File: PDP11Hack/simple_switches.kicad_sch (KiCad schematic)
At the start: 26 parts, among them SW1 SW_SPDT_XKB_DMx-xxxx-1, SW2 SW_SPDT_XKB_DMx-xxxx-1, SW3 SW_Push, SW4 SW_Push, SW5 SW_SPDT_XKB_DMx-xxxx-1, U11_17 74HCT00, U16 74HC14, U17 74HCT00, U18 74HCT00, U20_19 74LS74, U9 74HCT04

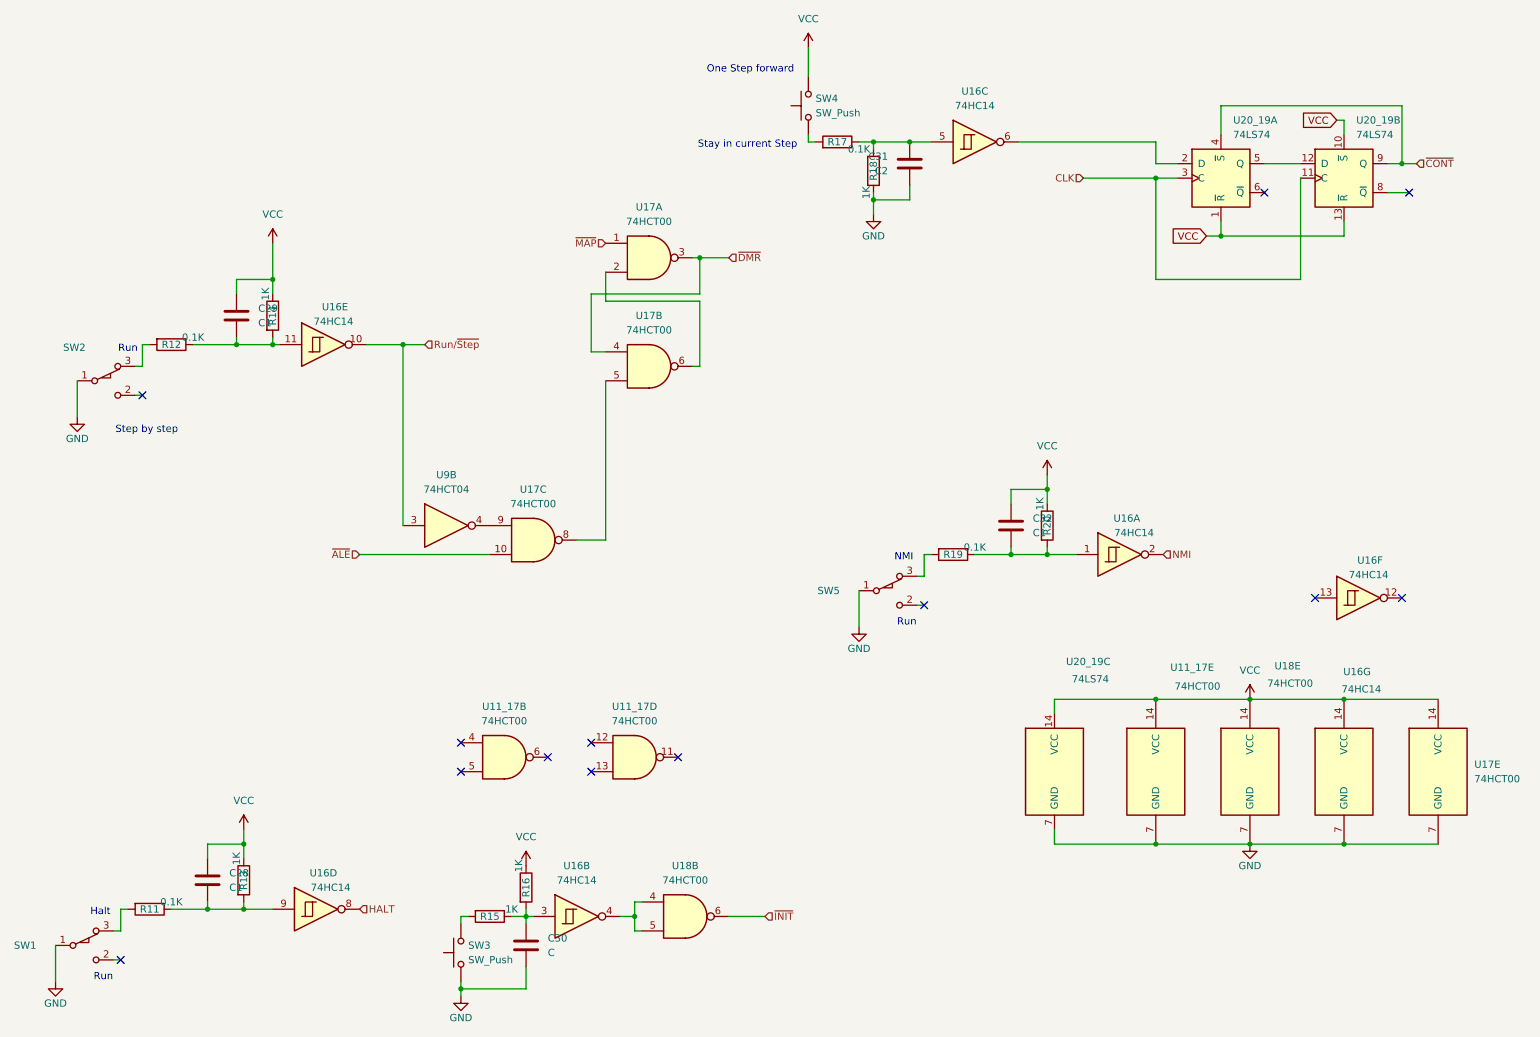
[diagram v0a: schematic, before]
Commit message: Corrections thanks to Peter Schranz on VCFED
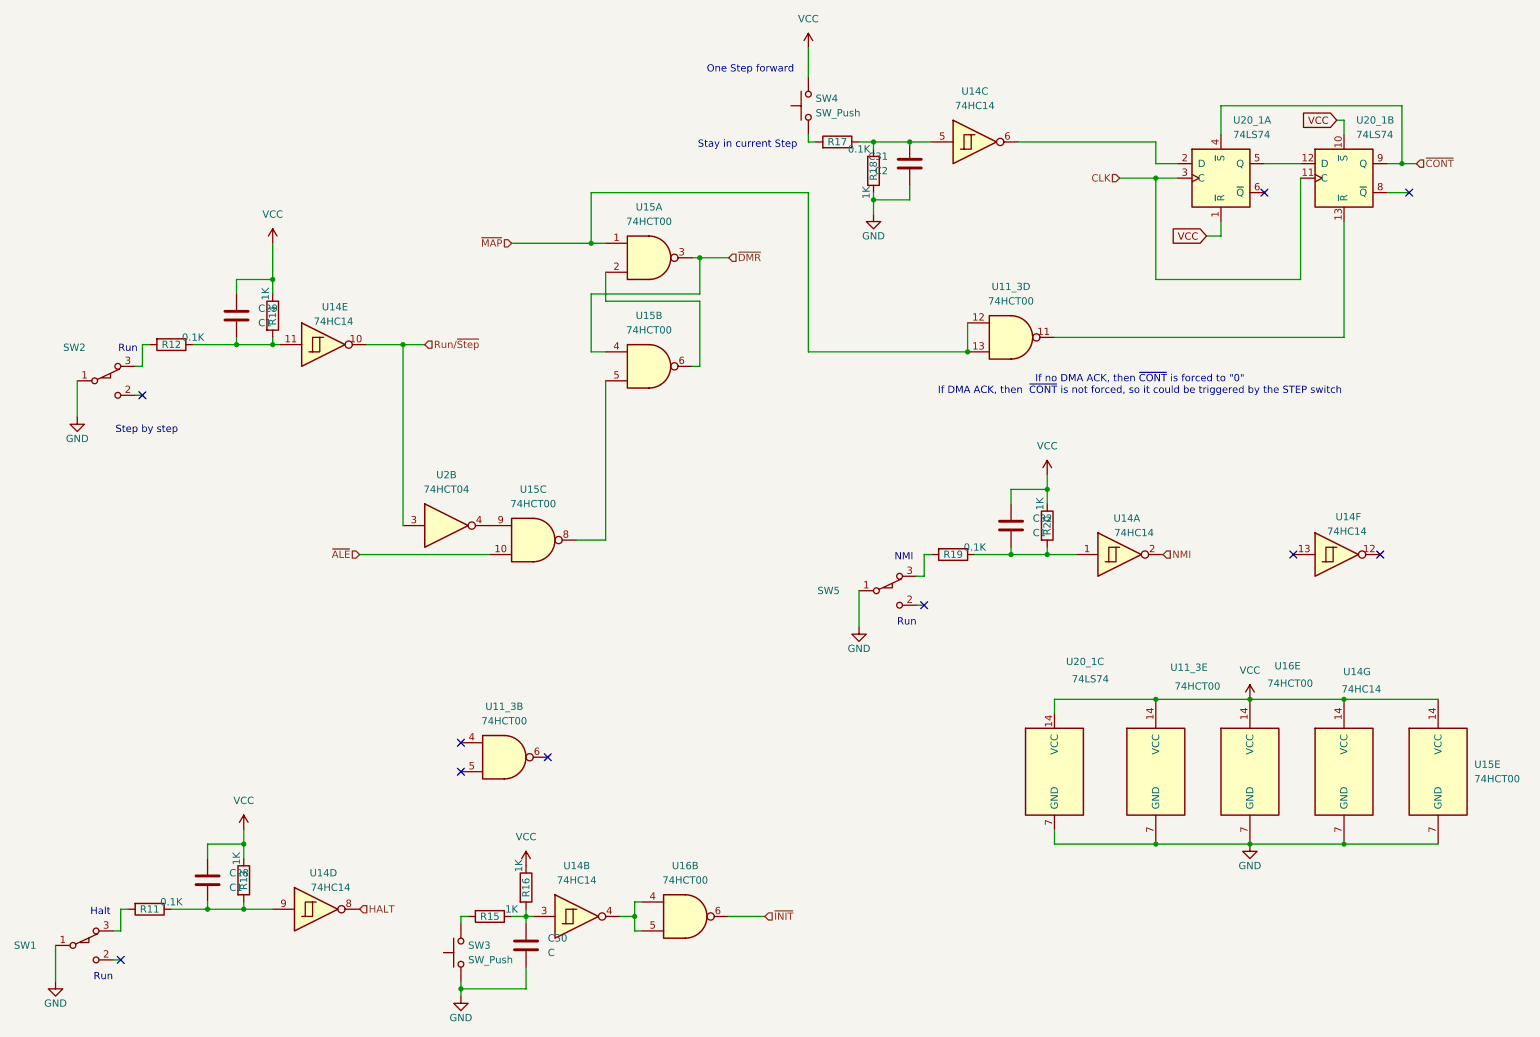
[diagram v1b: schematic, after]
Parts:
- removed unit 6 of U16
- added unit 6 of U14
- renumbered U11_17 to U11_3, U16 to U14, U17 to U15, U18 to U16, U9 to U2, U20_19 to U20_1
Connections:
- net VCC: no longer U20_1.13 (~{R})
- net ~{MAP}: now also U11_3.12, U11_3.13
- net at U11_3.11: now also U20_1.13 (~{R})
- no-connect marks 13 -> 10
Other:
- note added: "If no DMA ACK, then ~{CONT} is forced to "0" If DMA ACK, then ~{CONT} is not forced, so it could be triggered by the STEP switch"
- moved on the sheet: U11_3D

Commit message: Last update, PCB creation ready
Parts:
- added unit 1 of U11_3
- added unit 3 of U11_3
- added unit 4 of U15
- added unit 1 of U16
- added unit 4 of U16
- added unit 3 of U16
- SW1, SW2: footprint (none) -> Button_Switch_THT:SW_Lever_1P2T_NKK_GW12LxH
- SW5: footprint (none) -> Button_Switch_THT:SW_PUSH_E-Switch_FS5700DP_DPDT
- U11_3, U15, U16, U2, U20_1: footprint (none) -> Package_DIP:DIP-14_W7.62mm
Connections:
- net GND: now also U11_3.4, U11_3.5, U11_3.1, U11_3.10, U11_3.2, U11_3.9, U15.12, U15.13, U16.1, U16.10, U16.12, U16.13, U16.2, U16.9
- no-connect marks 10 -> 14
